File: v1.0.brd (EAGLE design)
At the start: 160 x 100 mm, 2 parts, among them U1 MCP23017-E/SO

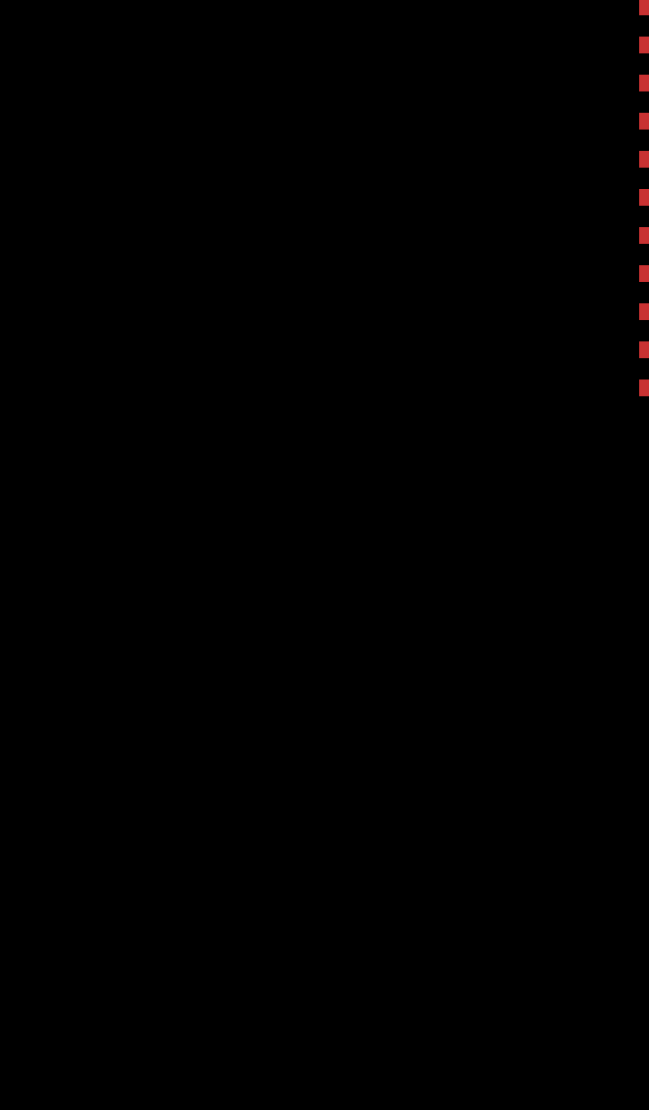
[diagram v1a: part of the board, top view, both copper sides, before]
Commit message: SPI CS expander
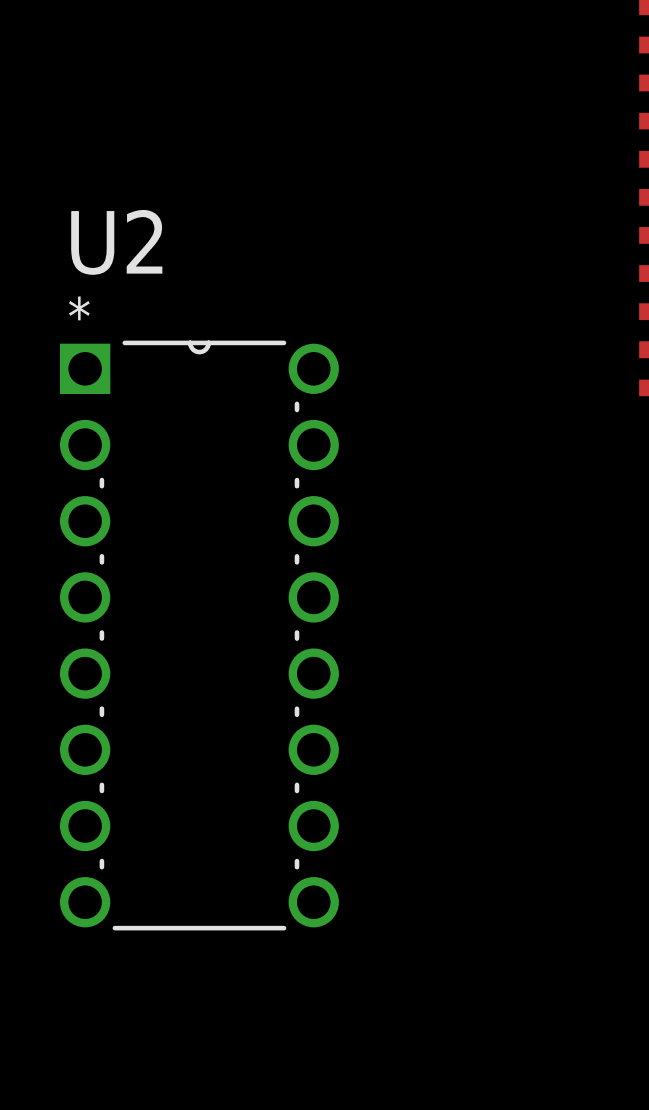
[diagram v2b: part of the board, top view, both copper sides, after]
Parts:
- added U2: 74HC139N, 74HC139N:DIP254P762X420-16
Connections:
- new net SPI0_CS0: PCB1.P$24, U2.1
- new net SPI0_CS1: PCB1.P$26, U2.15
- new net SPI_MISO: PCB1.P$21
- new net SPI_MOSI: PCB1.P$19
- new net SPI_SCLK: PCB1.P$23
- net +3V3: now also U1.18
- net +5V: now also U2.16
- net GND: now also U2.8
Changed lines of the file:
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@@
 <attribute name="SUPPLIER" value="Microchip" x="-116.84" y="30.48" size="1.778" layer="27" display="off"/>
+</element>
+<element name="U2" library="74HC139N" package="DIP254P762X420-16" value="74HC139N" x="-133.35" y="5.08">
+<attribute name="MPN" value="74HC139N" x="-133.35" y="5.08" size="1.778" layer="27" display="off"/>
+<attribute name="OC_FARNELL" value="380556" x="-133.35" y="5.08" size="1.778" layer="27" display="off"/>
+<attribute name="OC_NEWARK" value="07WX3674" x="-133.35" y="5.08" size="1.778" layer="27" display="off"/>
+<attribute name="PACKAGE" value="DIP-16" x="-133.35" y="5.08" size="1.778" layer="27" display="off"/>
+<attribute name="SUPPLIER" value="NXP" x="-133.35" y="5.08" size="1.778" layer="27" display="off"/>
 </element>
 </elements>
@@
 <contactref element="U1" pad="16"/>
 <contactref element="U1" pad="17"/>
+<contactref element="U2" pad="8"/>
+<wire x1="-121.3612" y1="27.305" x2="-140.97" y2="5.08" width="0" layer="19" extent="1-1"/>
 <wire x1="-112.3188" y1="24.765" x2="-121.3612" y2="27.305" width="0" layer="19" extent="1-1"/>
 <wire x1="-112.3188" y1="23.495" x2="-112.3188" y2="24.765" width="0" layer="19" extent="1-1"/>
 <wire x1="-112.3188" y1="22.225" x2="-112.3188" y2="23.495" width="0" layer="19" extent="1-1"/>
-<wire x1="5.9182" y1="64.0334" x2="-112.3188" y2="24.765" width="0" layer="19" extent="1-1"/>
+<wire x1="3.3782" y1="33.5534" x2="-112.3188" y2="24.765" width="0" layer="19" extent="1-1"/>
+<wire x1="3.3782" y1="38.6334" x2="3.3782" y2="33.5534" width="0" layer="19" extent="1-1"/>
+<wire x1="5.9182" y1="43.7134" x2="3.3782" y2="38.6334" width="0" layer="19" extent="1-1"/>
+<wire x1="3.3782" y1="51.3334" x2="5.9182" y2="43.7134" width="0" layer="19" extent="1-1"/>
+<wire x1="3.3782" y1="58.9534" x2="3.3782" y2="51.3334" width="0" layer="19" extent="1-1"/>
+<wire x1="5.9182" y1="64.0334" x2="3.3782" y2="58.9534" width="0" layer="19" extent="1-1"/>
 <wire x1="3.3782" y1="69.1134" x2="5.9182" y2="64.0334" width="0" layer="19" extent="1-1"/>
-<wire x1="3.3782" y1="58.9534" x2="5.9182" y2="64.0334" width="0" layer="19" extent="1-1"/>
-<wire x1="3.3782" y1="51.3334" x2="3.3782" y2="58.9534" width="0" layer="19" extent="1-1"/>
-<wire x1="5.9182" y1="43.7134" x2="3.3782" y2="51.3334" width="0" layer="19" extent="1-1"/>
-<wire x1="3.3782" y1="38.6334" x2="5.9182" y2="43.7134" width="0" layer="19" extent="1-1"/>
-<wire x1="3.3782" y1="33.5534" x2="3.3782" y2="38.6334" width="0" layer="19" extent="1-1"/>
 <wire x1="5.9182" y1="25.9334" x2="3.3782" y2="33.5534" width="0" layer="19" extent="1-1"/>
 </signal>
@@
 <contactref element="PCB1" pad="P$1"/>
 <contactref element="U1" pad="9"/>
-<wire x1="5.92" y1="74.18" x2="-121.3612" y2="28.575" width="0" layer="19" extent="1-1"/>
+<contactref element="U1" pad="18"/>
+<wire x1="-112.3188" y1="26.035" x2="-121.3612" y2="28.575" width="0" layer="19" extent="1-1"/>
+<wire x1="5.92" y1="74.18" x2="-112.3188" y2="26.035" width="0" layer="19" extent="1-1"/>
 </signal>
 <signal name="+5V">
 <contactref element="PCB1" pad="P$2"/>
 <contactref element="PCB1" pad="P$4"/>
-<wire x1="3.3782" y1="71.6534" x2="3.3782" y2="74.1934" width="0" layer="19" extent="1-1"/>
+<contactref element="U2" pad="16"/>
+<wire x1="3.3782" y1="71.6534" x2="-133.35" y2="22.86" width="0" layer="19" extent="1-1"/>
+<wire x1="3.3782" y1="74.1934" x2="3.3782" y2="71.6534" width="0" layer="19" extent="1-1"/>
 </signal>
 <signal name="SCL_3V3">
@@
 <wire x1="5.9182" y1="71.6534" x2="-121.3612" y2="23.495" width="0" layer="19" extent="1-1"/>
 </signal>
+<signal name="SPI_MOSI">
+<contactref element="PCB1" pad="P$19"/>
+</signal>
+<signal name="SPI_MISO">
+<contactref element="PCB1" pad="P$21"/>
+</signal>
+<signal name="SPI_SCLK">
+<contactref element="PCB1" pad="P$23"/>
+</signal>
+<signal name="SPI0_CS1">
+<contactref element="PCB1" pad="P$26"/>
+<contactref element="U2" pad="15"/>
+<wire x1="3.3782" y1="43.7134" x2="-133.35" y2="20.32" width="0" layer="19" extent="1-1"/>
+</signal>
+<signal name="SPI0_CS0">
+<contactref element="PCB1" pad="P$24"/>
+<contactref element="U2" pad="1"/>
+<wire x1="3.3782" y1="46.2534" x2="-140.97" y2="22.86" width="0" layer="19" extent="1-1"/>
+</signal>
 </signals>

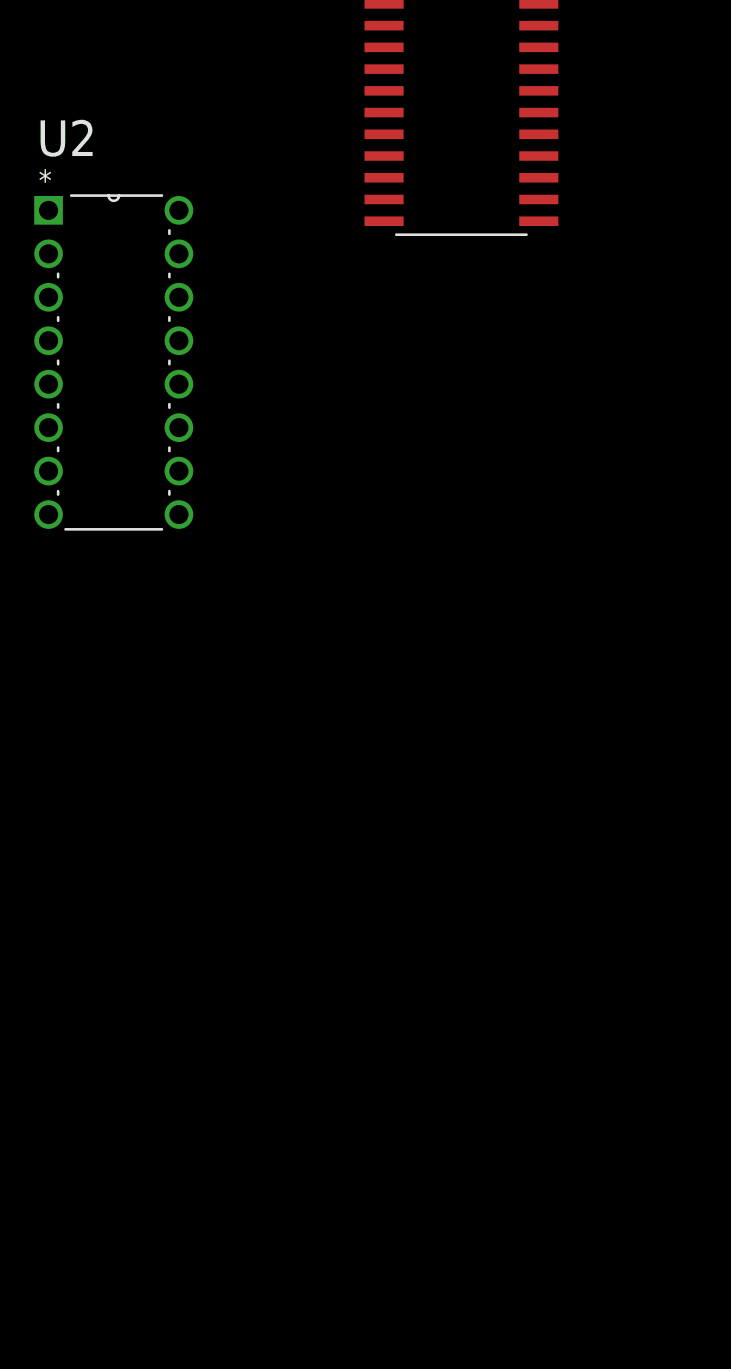
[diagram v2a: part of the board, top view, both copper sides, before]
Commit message: added SPI CS expander on it's own page
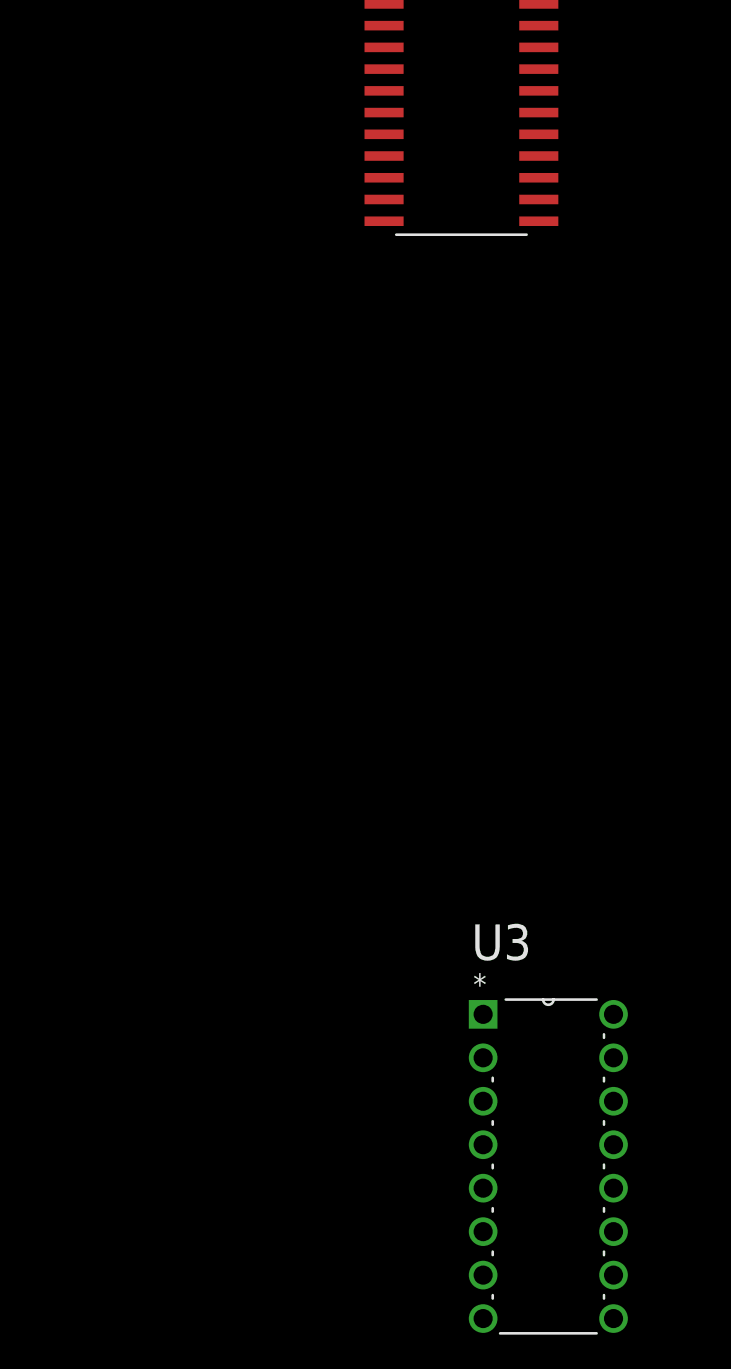
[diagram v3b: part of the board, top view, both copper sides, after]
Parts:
- removed U2: 74HC139N, 74HC139N:DIP254P762X420-16
- added U3: 74HC139N, 74HC139N:DIP254P762X420-16
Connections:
- net +5V: now also U3.16; no longer U2.16
- net GND: now also U3.8; no longer U2.8
- net SPI0_CS0: now also U3.1; no longer U2.1
- net SPI0_CS1: now also U3.15; no longer U2.15
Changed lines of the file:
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@@
 <attribute name="SUPPLIER" value="Microchip" x="-116.84" y="30.48" size="1.778" layer="27" display="off"/>
 </element>
-<element name="U2" library="74HC139N" package="DIP254P762X420-16" value="74HC139N" x="-133.35" y="5.08">
-<attribute name="MPN" value="74HC139N" x="-133.35" y="5.08" size="1.778" layer="27" display="off"/>
-<attribute name="OC_FARNELL" value="380556" x="-133.35" y="5.08" size="1.778" layer="27" display="off"/>
-<attribute name="OC_NEWARK" value="07WX3674" x="-133.35" y="5.08" size="1.778" layer="27" display="off"/>
-<attribute name="PACKAGE" value="DIP-16" x="-133.35" y="5.08" size="1.778" layer="27" display="off"/>
-<attribute name="SUPPLIER" value="NXP" x="-133.35" y="5.08" size="1.778" layer="27" display="off"/>
+<element name="U3" library="74HC139N" package="DIP254P762X420-16" value="74HC139N" x="-107.95" y="-41.91">
+<attribute name="MPN" value="74HC139N" x="-133.35" y="-6.35" size="1.778" layer="27" display="off"/>
+<attribute name="OC_FARNELL" value="380556" x="-133.35" y="-6.35" size="1.778" layer="27" display="off"/>
+<attribute name="OC_NEWARK" value="07WX3674" x="-133.35" y="-6.35" size="1.778" layer="27" display="off"/>
+<attribute name="PACKAGE" value="DIP-16" x="-133.35" y="-6.35" size="1.778" layer="27" display="off"/>
+<attribute name="SUPPLIER" value="NXP" x="-133.35" y="-6.35" size="1.778" layer="27" display="off"/>
 </element>
 </elements>
@@
 <contactref element="U1" pad="16"/>
 <contactref element="U1" pad="17"/>
-<contactref element="U2" pad="8"/>
-<wire x1="-121.3612" y1="27.305" x2="-140.97" y2="5.08" width="0" layer="19" extent="1-1"/>
-<wire x1="-112.3188" y1="24.765" x2="-121.3612" y2="27.305" width="0" layer="19" extent="1-1"/>
-<wire x1="-112.3188" y1="23.495" x2="-112.3188" y2="24.765" width="0" layer="19" extent="1-1"/>
-<wire x1="-112.3188" y1="22.225" x2="-112.3188" y2="23.495" width="0" layer="19" extent="1-1"/>
+<contactref element="U3" pad="8"/>
+<wire x1="-112.3188" y1="22.225" x2="-115.57" y2="-41.91" width="0" layer="19" extent="1-1"/>
+<wire x1="-112.3188" y1="23.495" x2="-112.3188" y2="22.225" width="0" layer="19" extent="1-1"/>
+<wire x1="-112.3188" y1="24.765" x2="-112.3188" y2="23.495" width="0" layer="19" extent="1-1"/>
+<wire x1="-121.3612" y1="27.305" x2="-112.3188" y2="24.765" width="0" layer="19" extent="1-1"/>
 <wire x1="3.3782" y1="33.5534" x2="-112.3188" y2="24.765" width="0" layer="19" extent="1-1"/>
 <wire x1="3.3782" y1="38.6334" x2="3.3782" y2="33.5534" width="0" layer="19" extent="1-1"/>
@@
 <contactref element="PCB1" pad="P$2"/>
 <contactref element="PCB1" pad="P$4"/>
-<contactref element="U2" pad="16"/>
-<wire x1="3.3782" y1="71.6534" x2="-133.35" y2="22.86" width="0" layer="19" extent="1-1"/>
+<contactref element="U3" pad="16"/>
+<wire x1="3.3782" y1="71.6534" x2="-107.95" y2="-24.13" width="0" layer="19" extent="1-1"/>
 <wire x1="3.3782" y1="74.1934" x2="3.3782" y2="71.6534" width="0" layer="19" extent="1-1"/>
 </signal>
@@
 <signal name="SPI0_CS1">
 <contactref element="PCB1" pad="P$26"/>
-<contactref element="U2" pad="15"/>
-<wire x1="3.3782" y1="43.7134" x2="-133.35" y2="20.32" width="0" layer="19" extent="1-1"/>
+<contactref element="U3" pad="15"/>
+<wire x1="3.3782" y1="43.7134" x2="-107.95" y2="-26.67" width="0" layer="19" extent="1-1"/>
 </signal>
 <signal name="SPI0_CS0">
 <contactref element="PCB1" pad="P$24"/>
-<contactref element="U2" pad="1"/>
-<wire x1="3.3782" y1="46.2534" x2="-140.97" y2="22.86" width="0" layer="19" extent="1-1"/>
+<contactref element="U3" pad="1"/>
+<wire x1="3.3782" y1="46.2534" x2="-115.57" y2="-24.13" width="0" layer="19" extent="1-1"/>
 </signal>
 </signals>

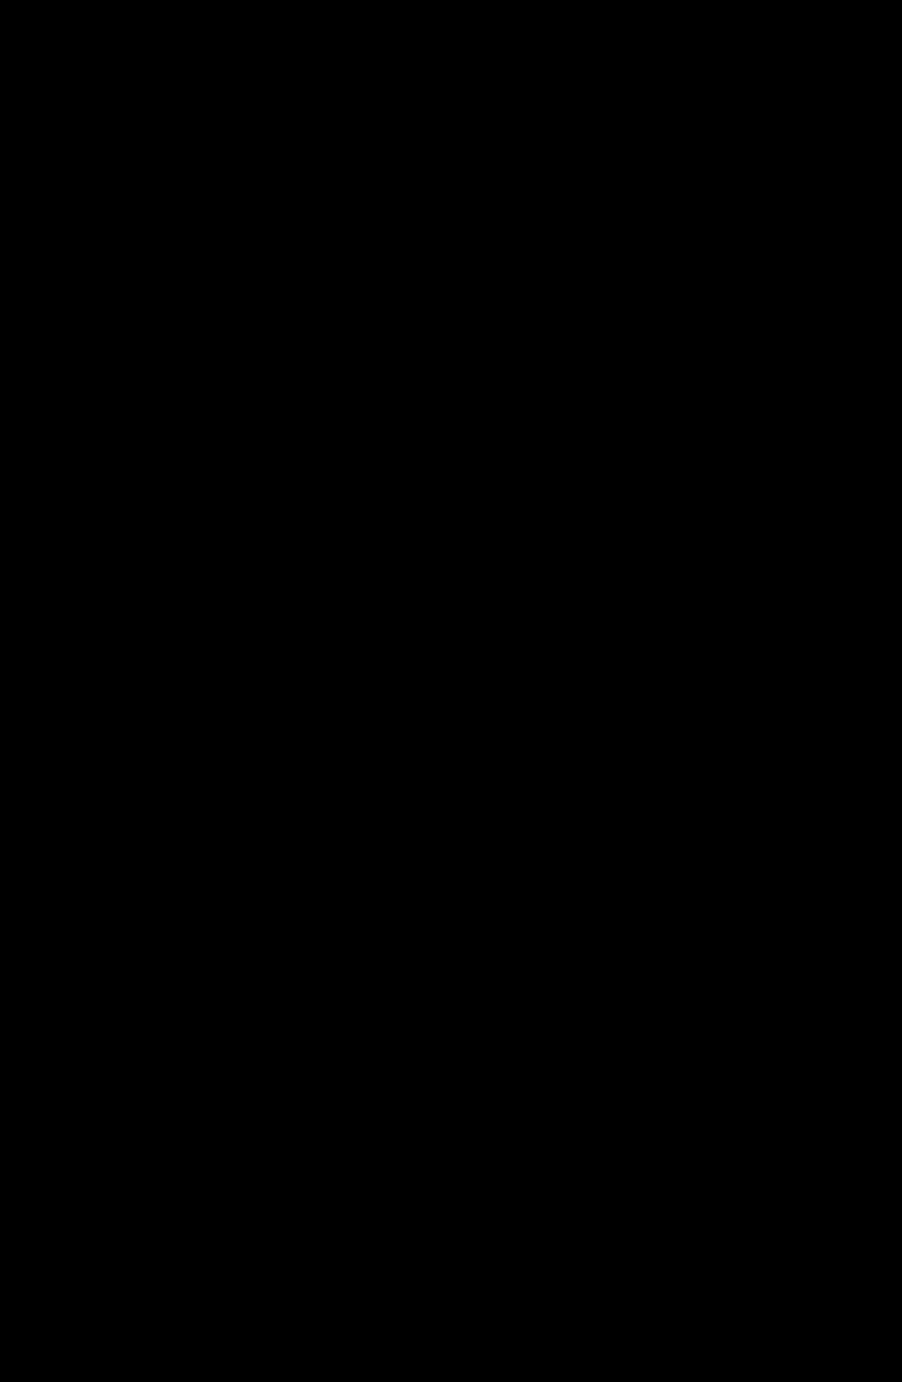
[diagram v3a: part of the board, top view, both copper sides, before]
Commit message: added power circuit
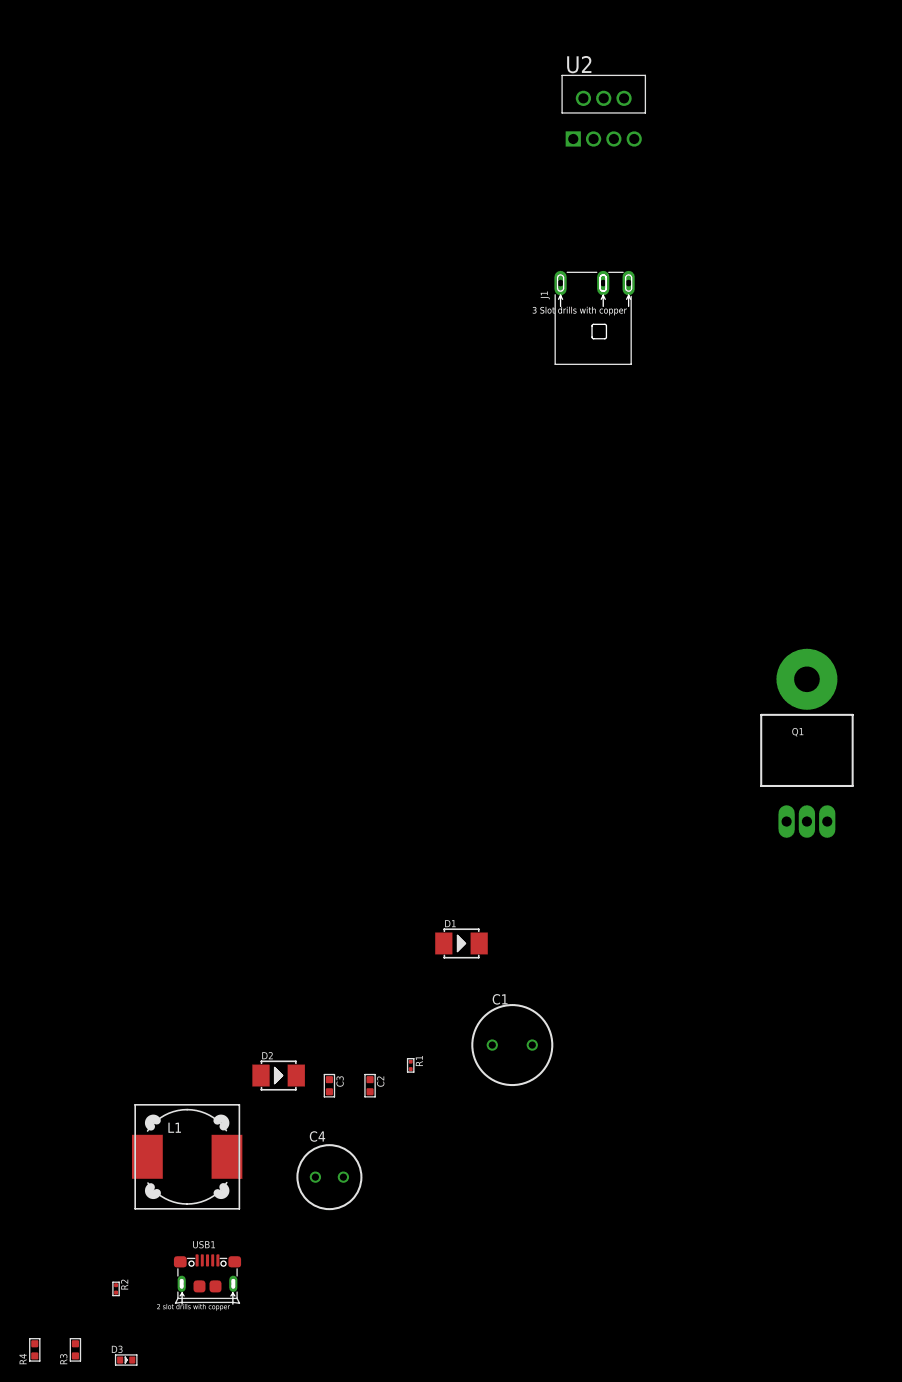
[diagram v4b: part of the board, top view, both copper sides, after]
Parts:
- added C1: CAP_TH_470UF_50V, Seeed-OPL-2017-01-Capacitor-akita:CAP_TH_P50_D100_POL
- added C2, C3: 100nf, Seeed-Capacitor-2016:C0603
- added C4: CAP_TH_220UF_25V, Seeed-OPL-2017-01-Capacitor-akita:CAP_TH_P35_D80_POL
- added D1, D2: 28V-5A, Seeed-Diode-2016:DO-214AA
- added D3: GREEN-0603, Seeed-LED-2016:LED-0603
- added J1: DC-044-A, Seeed-Connector -2016:DCJ3P-11.6X9.6X7.0MM
- added L1: DR125-330-R 33uH, inductors:DR125
- added Q1: IRF520NPBF, Seeed-Transistor-2016:TO-220
- added R1, R2: 10K 1/16W, Seeed-Resistor-2016:R0402
- added R3: 1K, Seeed-Resistor-2016:R0603
- added R4: 100K, Seeed-Resistor-2016:R0603
- added U2: LM2599T-5.0, LM2599T:TO127P470X1016X1740-7P
- added USB1: ST-USB-001G, Seeed-Connector -2016:MICRO-USB5+4P-SMD-0.65-B
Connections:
- new net +24V_UNREG_IN: D1.+, J1.+
- new net +5V/1: Q1.3, R3.1, USB1.1
- new net +5V_REG_OUT: C4.P$M, L1.2, Q1.1, R1.1, R2.1, U2.6
- new net GNDA: C1.P$M, C2.2, C3.2, C4.P$P, D2.+, D3.-, J1.-, J1.CDN, Q1.2, Q1.HEAT, R4.2, U2.4, USB1.5, USB1.S1, USB1.S2, USB1.S3, USB1.S4, USB1.S5, USB1.S6
- new net N$1: D3.+, R3.2
- new net N$2: C1.P$P, D1.-, U2.1
- new net N$3: C2.1, U2.7
- new net N$4: D2.-, L1.1, U2.2
- new net N$5: R4.1, USB1.4
- new net N$6: C3.1, U2.5
- new net N$7: R1.2, U2.3
- new net SCLK: PCB1.P$7
- new net UART_RX: PCB1.P$10
- new net UART_TDX: PCB1.P$8
